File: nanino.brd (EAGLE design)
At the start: 68.6 x 53.3 mm, 19 parts, among them IC1 ATMEGA168-20P

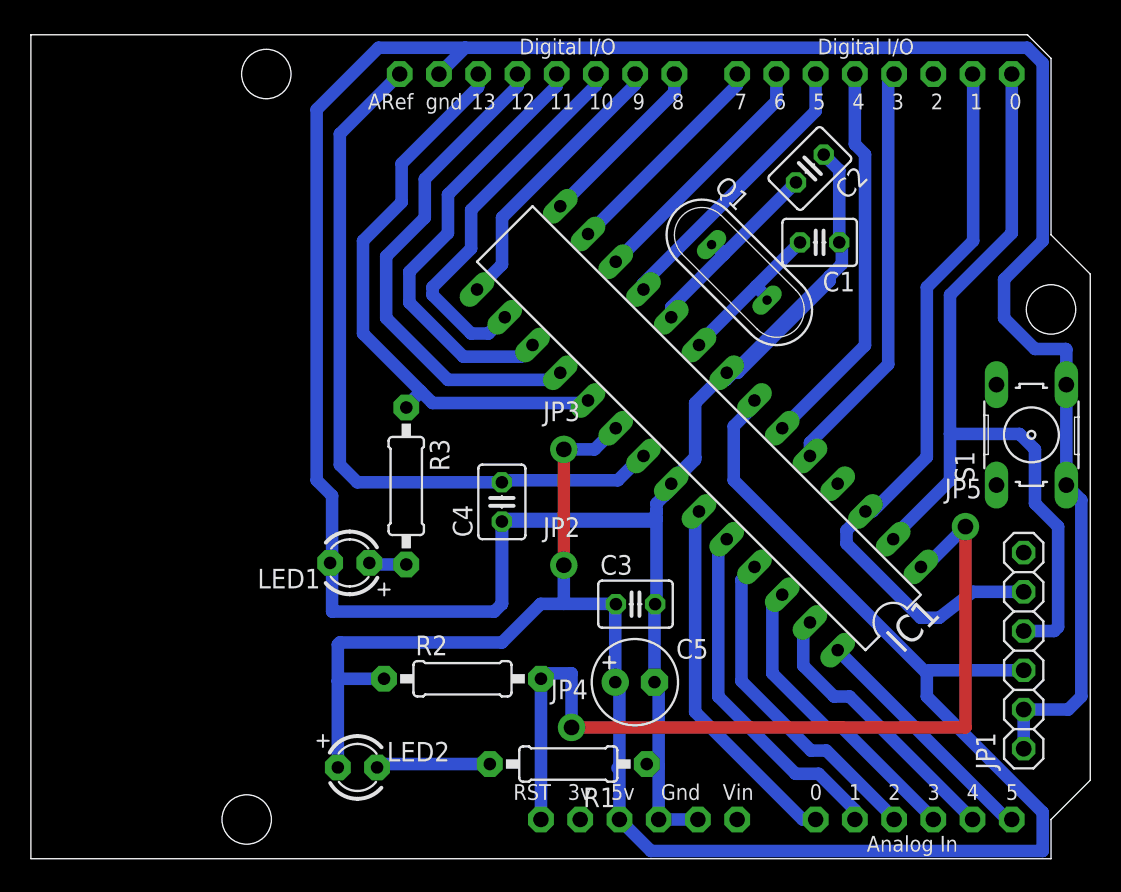
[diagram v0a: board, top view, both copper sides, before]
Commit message: Added missing D2 Pin
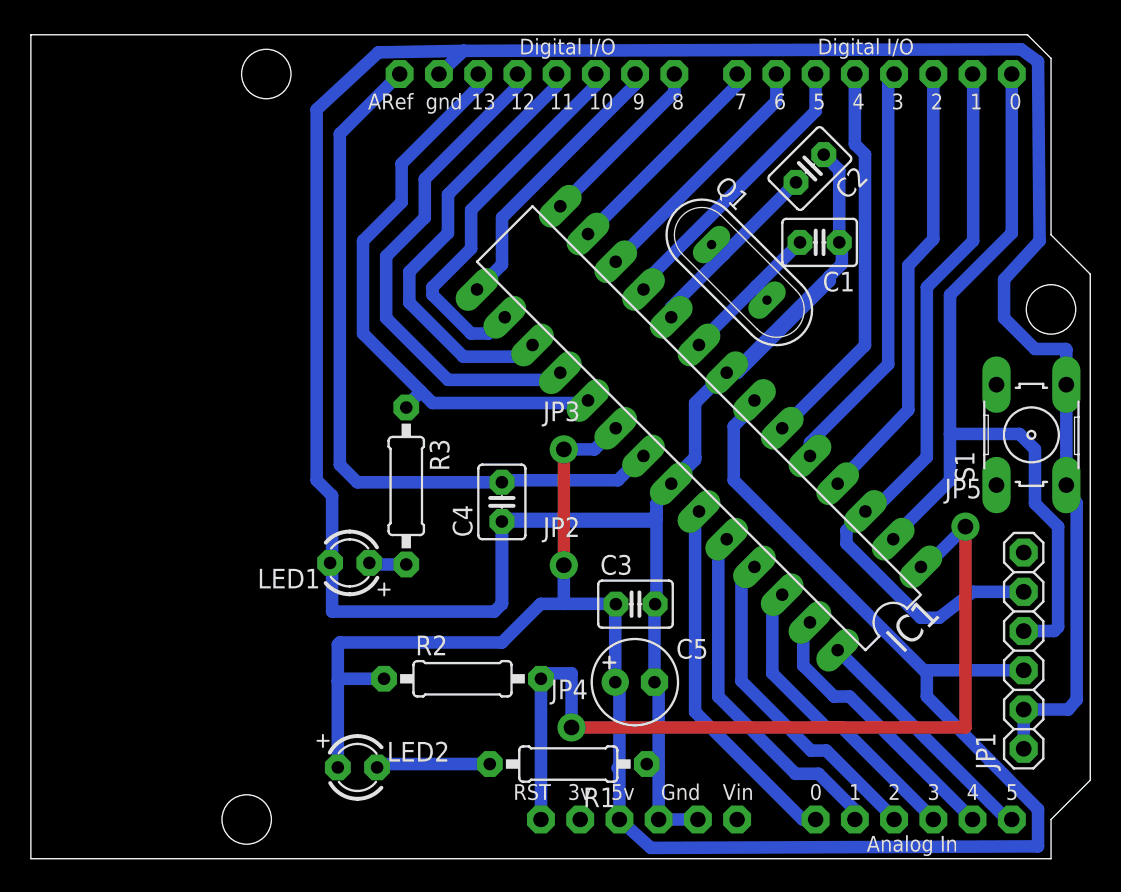
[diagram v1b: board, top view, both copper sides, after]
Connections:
- net D2: now also IC1.4
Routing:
- net D2: track 0.00 -> 29.0 mm
- net GND: track 244.8 -> 243.6 mm
- net VCC: track 131.2 -> 130.4 mm
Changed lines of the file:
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@@
 <setting verticaltext="up"/>
 </settings>
-<grid distance="0.5" unitdist="mm" unit="mm" style="lines" multiple="1" display="no" altdistance="0.025" altunitdist="inch" altunit="mm"/>
+<grid distance="0.1" unitdist="mm" unit="mm" style="lines" multiple="1" display="no" altdistance="0.025" altunitdist="inch" altunit="mm"/>
 <layers>
 <layer number="1" name="Top" color="4" fill="1" visible="yes" active="yes"/>
@@
 <param name="mtCopper" value="0.035mm 0.035mm 0.035mm 0.035mm 0.035mm 0.035mm 0.035mm 0.035mm 0.035mm 0.035mm 0.035mm 0.035mm 0.035mm 0.035mm 0.035mm 0.035mm"/>
 <param name="mtIsolate" value="1.5mm 0.15mm 0.2mm 0.15mm 0.2mm 0.15mm 0.2mm 0.15mm 0.2mm 0.15mm 0.2mm 0.15mm 0.2mm 0.15mm 0.2mm"/>
-<param name="mdWireWire" value="8mil"/>
-<param name="mdWirePad" value="8mil"/>
-<param name="mdWireVia" value="8mil"/>
+<param name="mdWireWire" value="12mil"/>
+<param name="mdWirePad" value="12mil"/>
+<param name="mdWireVia" value="12mil"/>
 <param name="mdPadPad" value="8mil"/>
 <param name="mdPadVia" value="8mil"/>
@@
 <param name="rvMicroViaOuter" value="0.25"/>
 <param name="rvMicroViaInner" value="0.25"/>
-<param name="rlMinPadTop" value="10mil"/>
-<param name="rlMaxPadTop" value="20mil"/>
-<param name="rlMinPadInner" value="10mil"/>
-<param name="rlMaxPadInner" value="20mil"/>
-<param name="rlMinPadBottom" value="10mil"/>
-<param name="rlMaxPadBottom" value="20mil"/>
-<param name="rlMinViaOuter" value="8mil"/>
-<param name="rlMaxViaOuter" value="20mil"/>
-<param name="rlMinViaInner" value="8mil"/>
-<param name="rlMaxViaInner" value="20mil"/>
-<param name="rlMinMicroViaOuter" value="4mil"/>
-<param name="rlMaxMicroViaOuter" value="20mil"/>
-<param name="rlMinMicroViaInner" value="4mil"/>
-<param name="rlMaxMicroViaInner" value="20mil"/>
+<param name="rlMinPadTop" value="16mil"/>
+<param name="rlMaxPadTop" value="16mil"/>
+<param name="rlMinPadInner" value="16mil"/>
+<param name="rlMaxPadInner" value="16mil"/>
+<param name="rlMinPadBottom" value="16mil"/>
+<param name="rlMaxPadBottom" value="16mil"/>
+<param name="rlMinViaOuter" value="12mil"/>
+<param name="rlMaxViaOuter" value="16mil"/>
+<param name="rlMinViaInner" value="12mil"/>
+<param name="rlMaxViaInner" value="16mil"/>
+<param name="rlMinMicroViaOuter" value="8mil"/>
+<param name="rlMaxMicroViaOuter" value="12mil"/>
+<param name="rlMinMicroViaInner" value="8mil"/>
+<param name="rlMaxMicroViaInner" value="12mil"/>
 <param name="psTop" value="-1"/>
 <param name="psBottom" value="-1"/>
@@
 <wire x1="65" y1="33" x2="63" y2="35" width="0.8128" layer="16"/>
 <wire x1="63" y1="35" x2="63" y2="37.5" width="0.8128" layer="16"/>
-<wire x1="63" y1="37.5" x2="65.5" y2="40" width="0.8128" layer="16"/>
-<wire x1="65.5" y1="40" x2="65.5" y2="51.5" width="0.8128" layer="16"/>
-<wire x1="65.5" y1="51.5" x2="64.5" y2="52.5" width="0.8128" layer="16"/>
-<wire x1="64.5" y1="52.5" x2="28.116" y2="52.5" width="0.8128" layer="16"/>
-<wire x1="28.116" y1="52.5" x2="26.416" y2="50.8" width="0.8128" layer="16"/>
+<wire x1="63" y1="37.5" x2="65.3" y2="40" width="0.8128" layer="16"/>
+<wire x1="65.3" y1="40" x2="65.2" y2="51.6" width="0.8128" layer="16"/>
+<wire x1="65.2" y1="51.6" x2="64.1" y2="52.4" width="0.8128" layer="16"/>
+<wire x1="64.1" y1="52.4" x2="28.016" y2="52.3" width="0.8128" layer="16"/>
+<wire x1="28.016" y1="52.3" x2="26.416" y2="50.8" width="0.8128" layer="16"/>
 <wire x1="40.64" y1="2.54" x2="40.64" y2="6" width="0.8128" layer="16"/>
 <wire x1="40.64" y1="6" x2="40.64" y2="11.16" width="0.8128" layer="16"/>
@@
 <wire x1="64.27" y1="7.12" x2="64.27" y2="9.66" width="0.8128" layer="16"/>
 <wire x1="64.27" y1="9.66" x2="67.16" y2="9.66" width="0.8128" layer="16"/>
-<wire x1="67.16" y1="9.66" x2="68" y2="10.5" width="0.8128" layer="16"/>
-<wire x1="68" y1="10.5" x2="68" y2="23.2194" width="0.8128" layer="16"/>
-<wire x1="68" y1="23.2194" x2="67.0306" y2="24.1888" width="0.8128" layer="16"/>
+<wire x1="67.16" y1="9.66" x2="67.7" y2="10.3" width="0.8128" layer="16"/>
+<wire x1="67.7" y1="10.3" x2="67.7" y2="23.0194" width="0.8128" layer="16"/>
+<wire x1="67.7" y1="23.0194" x2="67.0306" y2="24.1888" width="0.8128" layer="16"/>
 <wire x1="30.49" y1="21.83" x2="30.49" y2="16.49" width="0.8128" layer="16"/>
 <wire x1="30.49" y1="16.49" x2="30" y2="16" width="0.8128" layer="16"/>
@@
 <wire x1="19.5" y1="23.5" x2="18.5" y2="24.5" width="0.8128" layer="16"/>
 <wire x1="18.5" y1="24.5" x2="18.5" y2="48.5" width="0.8128" layer="16"/>
-<wire x1="18.5" y1="48.5" x2="22.5" y2="52.5" width="0.8128" layer="16"/>
-<wire x1="22.5" y1="52.5" x2="28.116" y2="52.5" width="0.8128" layer="16"/>
+<wire x1="18.5" y1="48.5" x2="22.5" y2="52.2" width="0.8128" layer="16"/>
+<wire x1="22.5" y1="52.2" x2="28.016" y2="52.3" width="0.8128" layer="16"/>
 </signal>
 <signal name="RESET">
@@
 <wire x1="45.5" y1="24.5" x2="58" y2="12" width="0.8128" layer="16"/>
 <wire x1="58" y1="12" x2="58" y2="10.5" width="0.8128" layer="16"/>
-<wire x1="58" y1="10.5" x2="65.5" y2="3" width="0.8128" layer="16"/>
-<wire x1="65.5" y1="3" x2="65.5" y2="0.5" width="0.8128" layer="16"/>
-<wire x1="65.5" y1="0.5" x2="40.14" y2="0.5" width="0.8128" layer="16"/>
-<wire x1="40.14" y1="0.5" x2="38.1" y2="2.54" width="0.8128" layer="16"/>
+<wire x1="58" y1="10.5" x2="65.2" y2="3.2" width="0.8128" layer="16"/>
+<wire x1="65.2" y1="3.2" x2="65.2" y2="0.8" width="0.8128" layer="16"/>
+<wire x1="65.2" y1="0.8" x2="40.14" y2="0.7" width="0.8128" layer="16"/>
+<wire x1="40.14" y1="0.7" x2="38.1" y2="2.54" width="0.8128" layer="16"/>
 <wire x1="64.27" y1="12.2" x2="58.2" y2="12.2" width="0.8128" layer="16"/>
 <wire x1="58.2" y1="12.2" x2="58" y2="12" width="0.8128" layer="16"/>
@@
 <signal name="D2">
 <contactref element="U$1" pad="D2"/>
+<contactref element="IC1" pad="4"/>
+<wire x1="58.42" y1="50.8" x2="58.42" y2="40.12" width="0.8128" layer="16"/>
+<wire x1="58.42" y1="40.12" x2="56.8" y2="38.4" width="0.8128" layer="16"/>
+<wire x1="56.8" y1="38.4" x2="56.8" y2="29.04764375" width="0.8128" layer="16"/>
+<wire x1="56.8" y1="29.04764375" x2="52.230253125" y2="24.277896875" width="0.8128" layer="16"/>
 </signal>
 <signal name="D3">

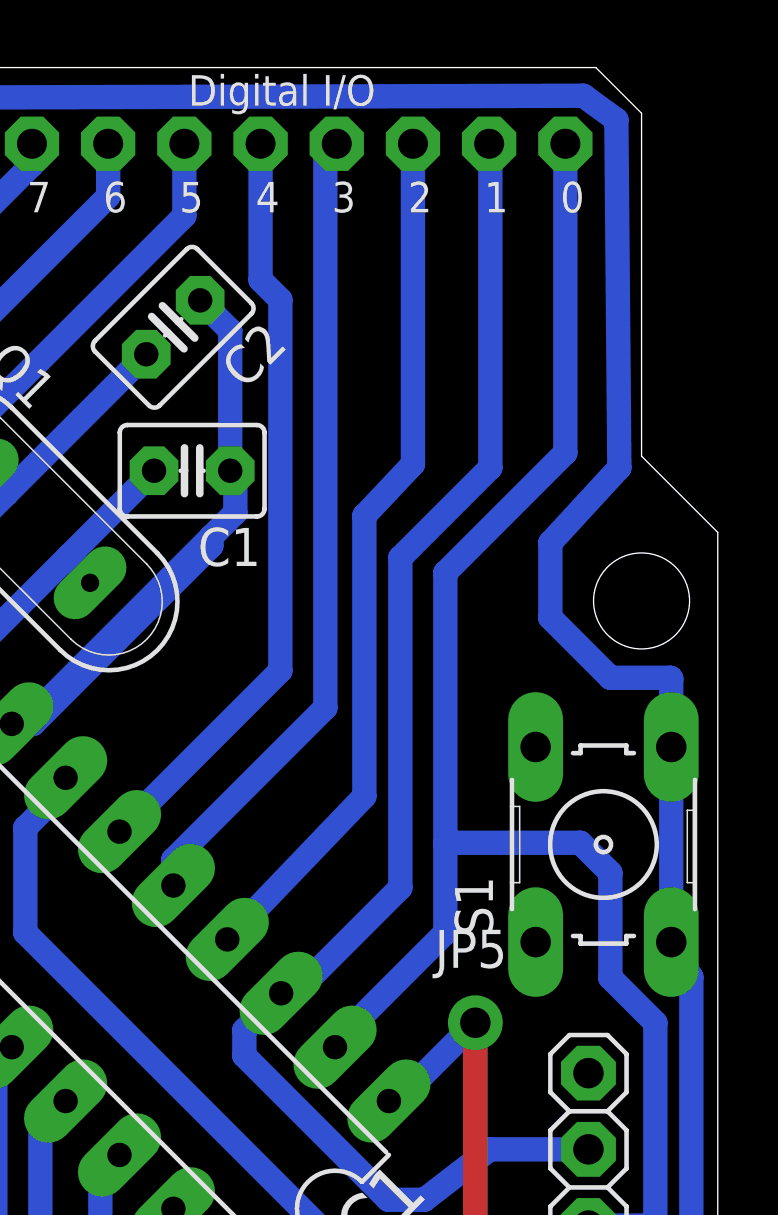
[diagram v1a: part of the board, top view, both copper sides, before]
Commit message: Fixed Reset Button Wire
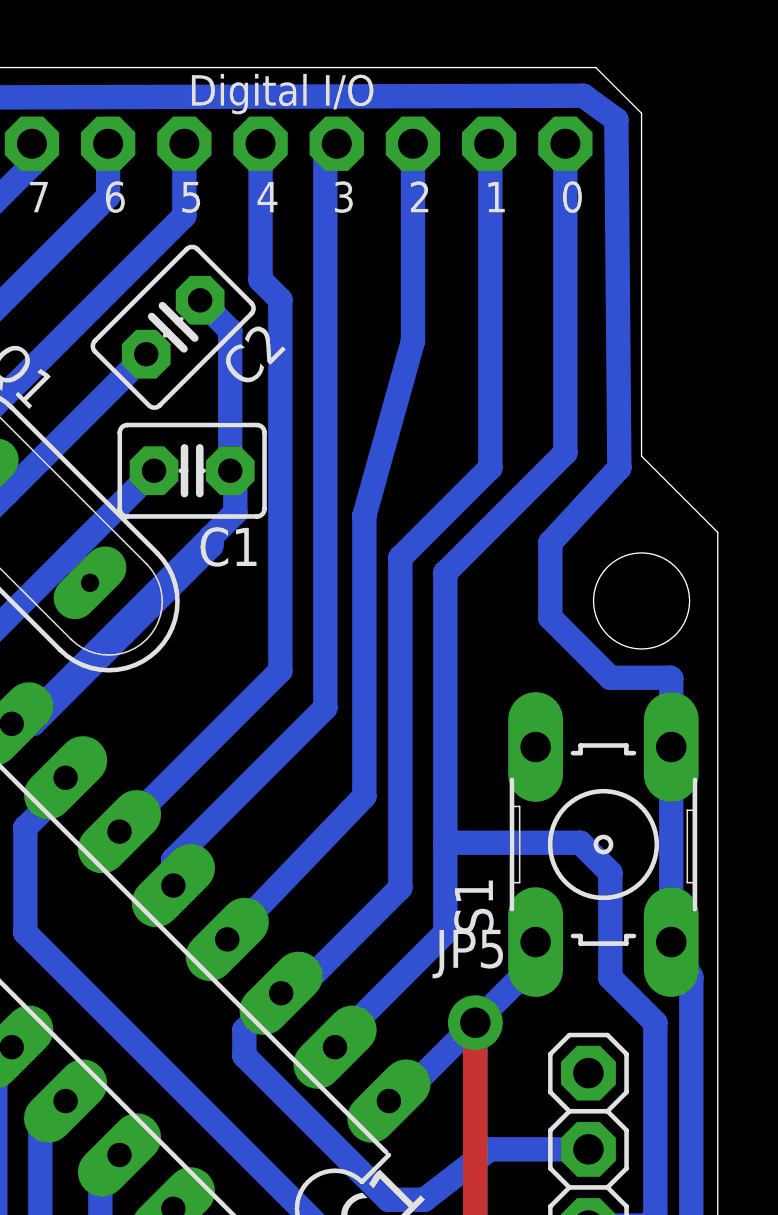
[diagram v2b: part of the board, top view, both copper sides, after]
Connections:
- net RESET: now also S1.1
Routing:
- net RESET: track 57.2 -> 60.7 mm
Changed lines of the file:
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@@
 <wire x1="60.5" y1="8.5" x2="60.5" y2="21.5" width="0.8128" layer="1"/>
 <wire x1="35" y1="8.5" x2="35" y2="12" width="0.8128" layer="16"/>
+<contactref element="S1" pad="1"/>
+<wire x1="62.5094" y1="24.1888" x2="62.5094" y2="23.5094" width="0.8128" layer="16"/>
+<wire x1="62.5094" y1="23.5094" x2="60.5" y2="21.5" width="0.8128" layer="16"/>
 </signal>
 <signal name="N$4">
@@
 <contactref element="U$1" pad="D2"/>
 <contactref element="IC1" pad="4"/>
-<wire x1="58.42" y1="50.8" x2="58.42" y2="40.12" width="0.8128" layer="16"/>
-<wire x1="58.42" y1="40.12" x2="56.8" y2="38.4" width="0.8128" layer="16"/>
+<wire x1="58.42" y1="50.8" x2="58.42" y2="44.22" width="0.8128" layer="16"/>
+<wire x1="58.42" y1="44.22" x2="56.8" y2="38.4" width="0.8128" layer="16"/>
 <wire x1="56.8" y1="38.4" x2="56.8" y2="29.04764375" width="0.8128" layer="16"/>
 <wire x1="56.8" y1="29.04764375" x2="52.230253125" y2="24.277896875" width="0.8128" layer="16"/>
